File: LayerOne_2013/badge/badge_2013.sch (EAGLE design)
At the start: 125 parts, among them CON2 EXT, CON6 J8, CON8 J3, IC1 SLICE_NOSHIFT_TLC5947HTSSOP32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, IC3 SLICE_NOSHIFT_TLC5947HTSSOP32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, IC4 TL064D, K1 5-XX, K2 5-XX, K3 5-XX, K4 5-XX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

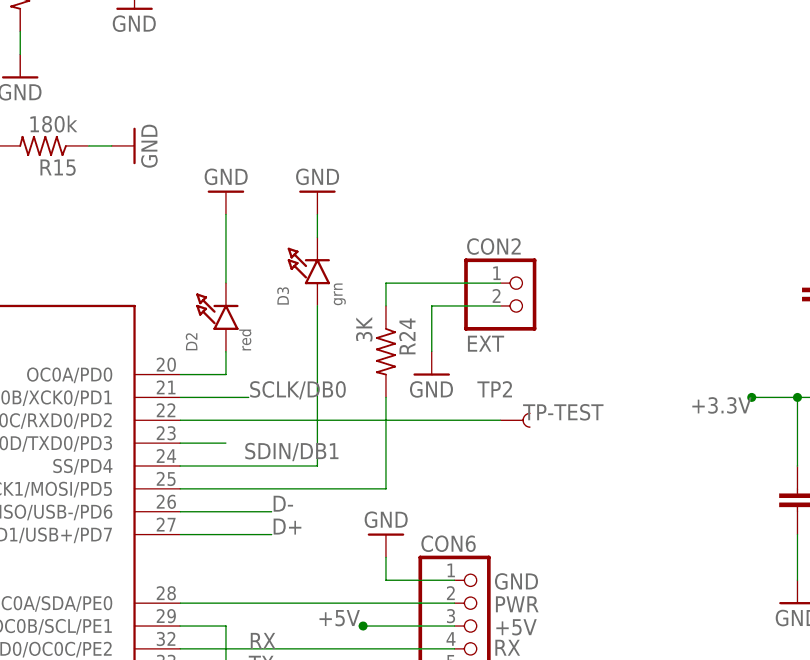
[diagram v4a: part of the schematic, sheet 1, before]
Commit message: 
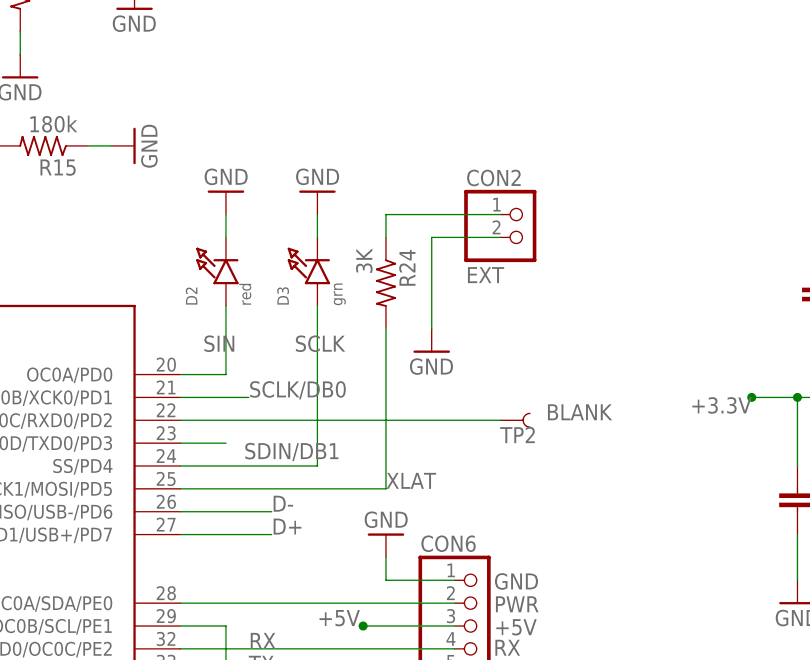
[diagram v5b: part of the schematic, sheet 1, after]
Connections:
- removed net N$19: IC2.XCK1/MOSI/PD5, R24.2
- removed net N$21: D2.A, IC2.OC0A/PD0
- removed net N$22: D3.A, IC2.SS/PD4
- removed net TP-TEST: IC2.OC0C/RXD0/PD2, TP2.1
- net BLANK: now also IC2.OC0C/RXD0/PD2, TP2.1
- net SCLK: now also D3.A, IC2.SS/PD4
- net SIN: now also D2.A, IC2.OC0A/PD0
- net XLAT: now also IC2.XCK1/MOSI/PD5, R24.2
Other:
- moved on the sheet: CON2, D2, R24
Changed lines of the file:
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@@
 </instance>
 <instance part="+3.3V" gate="1" x="246.38" y="86.36"/>
-<instance part="CON2" gate="G$1" x="241.3" y="137.16"/>
+<instance part="CON2" gate="G$1" x="241.3" y="144.78"/>
 <instance part="C1" gate="G$1" x="332.74" y="170.18" rot="R180"/>
 <instance part="C3" gate="G$1" x="93.98" y="226.06" rot="R270"/>
@@
 <instance part="CH1" gate="G$1" x="264.16" y="215.9"/>
 <instance part="TP1" gate="G$1" x="83.82" y="193.04"/>
-<instance part="TP2" gate="G$1" x="238.76" y="124.46"/>
+<instance part="TP2" gate="G$1" x="238.76" y="124.46" smashed="yes">
+<attribute name="NAME" x="238.76" y="121.92" size="1.778" layer="95"/>
+<attribute name="VALUE" x="236.22" y="121.92" size="1.778" layer="96"/>
+</instance>
 <instance part="Z1" gate="G$1" x="93.98" y="114.3" rot="MR0"/>
 <instance part="GND7" gate="1" x="99.06" y="99.06"/>
 <instance part="GND8" gate="1" x="78.74" y="129.54" rot="R180"/>
-<instance part="D2" gate="G$1" x="208.28" y="137.16" rot="R90"/>
+<instance part="D2" gate="G$1" x="208.28" y="142.24" rot="R90"/>
 <instance part="D3" gate="G$1" x="218.44" y="142.24" rot="R90"/>
 <instance part="GND9" gate="1" x="208.28" y="149.86" rot="R180"/>
@@
 <instance part="C23" gate="G$1" x="66.04" y="43.18" rot="R270"/>
 <instance part="GND40" gate="1" x="48.26" y="50.8"/>
-<instance part="GND41" gate="1" x="231.14" y="129.54"/>
+<instance part="GND41" gate="1" x="231.14" y="132.08"/>
 <instance part="X2" gate="G$1" x="121.92" y="60.96" smashed="yes" rot="R90">
 <attribute name="VALUE" x="137.668" y="59.182" size="1.778" layer="96" rot="R180"/>
@@
 <instance part="GND47" gate="1" x="312.42" y="187.96" rot="R270"/>
 <instance part="SJ1" gate="1" x="269.24" y="91.44"/>
-<instance part="R24" gate="G$1" x="226.06" y="132.08" rot="R270"/>
+<instance part="R24" gate="G$1" x="226.06" y="139.7" rot="R270"/>
 <instance part="PDI" gate="G$1" x="134.62" y="147.32" rot="R90"/>
 <instance part="R22" gate="G$1" x="81.28" y="33.02" rot="R270"/>
@@
 <segment>
 <pinref part="D2" gate="G$1" pin="C"/>
-<wire x1="208.28" y1="139.7" x2="208.28" y2="147.32" width="0.1524" layer="91"/>
+<wire x1="208.28" y1="144.78" x2="208.28" y2="147.32" width="0.1524" layer="91"/>
 <pinref part="GND9" gate="1" pin="GND"/>
 </segment>
@@
 <segment>
 <pinref part="CON2" gate="G$1" pin="2"/>
-<wire x1="238.76" y1="137.16" x2="231.14" y2="137.16" width="0.1524" layer="91"/>
-<wire x1="231.14" y1="137.16" x2="231.14" y2="132.08" width="0.1524" layer="91"/>
+<wire x1="238.76" y1="144.78" x2="231.14" y2="144.78" width="0.1524" layer="91"/>
+<wire x1="231.14" y1="144.78" x2="231.14" y2="134.62" width="0.1524" layer="91"/>
 <pinref part="GND41" gate="1" pin="GND"/>
 </segment>
@@
 </segment>
 </net>
-<net name="N$19" class="0">
+<net name="XLAT" class="0">
 <segment>
 <pinref part="IC2" gate="G$1" pin="XCK1/MOSI/PD5"/>
 <wire x1="203.2" y1="116.84" x2="226.06" y2="116.84" width="0.1524" layer="91"/>
 <pinref part="R24" gate="G$1" pin="2"/>
-<wire x1="226.06" y1="127" x2="226.06" y2="116.84" width="0.1524" layer="91"/>
+<wire x1="226.06" y1="134.62" x2="226.06" y2="116.84" width="0.1524" layer="91"/>
+<label x="226.06" y="116.84" size="1.778" layer="95"/>
 </segment>
 </net>
@@
 </segment>
 </net>
-<net name="N$21" class="0">
+<net name="SIN" class="0">
 <segment>
 <pinref part="D2" gate="G$1" pin="A"/>
 <pinref part="IC2" gate="G$1" pin="OC0A/PD0"/>
-<wire x1="208.28" y1="132.08" x2="208.28" y2="129.54" width="0.1524" layer="91"/>
+<wire x1="208.28" y1="137.16" x2="208.28" y2="129.54" width="0.1524" layer="91"/>
 <wire x1="208.28" y1="129.54" x2="203.2" y2="129.54" width="0.1524" layer="91"/>
-</segment>
-</net>
-<net name="N$22" class="0">
+<label x="205.74" y="132.08" size="1.778" layer="95"/>
+</segment>
+</net>
+<net name="SCLK" class="0">
 <segment>
 <pinref part="D3" gate="G$1" pin="A"/>
@@
 <wire x1="218.44" y1="137.16" x2="218.44" y2="119.38" width="0.1524" layer="91"/>
 <wire x1="218.44" y1="119.38" x2="203.2" y2="119.38" width="0.1524" layer="91"/>
+<label x="215.9" y="132.08" size="1.778" layer="95"/>
 </segment>
 </net>
@@
 </segment>
 </net>
-<net name="TP-TEST" class="0">
+<net name="BLANK" class="0">
 <segment>
 <pinref part="IC2" gate="G$1" pin="OC0C/RXD0/PD2"/>
 <pinref part="TP2" gate="G$1" pin="1"/>
 <wire x1="203.2" y1="124.46" x2="238.76" y2="124.46" width="0.1524" layer="91"/>
-<label x="241.3" y="124.46" size="1.778" layer="95"/>
+<label x="243.84" y="124.46" size="1.778" layer="95"/>
 </segment>
 </net>
@@
 <segment>
 <pinref part="CON2" gate="G$1" pin="1"/>
-<wire x1="238.76" y1="139.7" x2="226.06" y2="139.7" width="0.1524" layer="91"/>
+<wire x1="238.76" y1="147.32" x2="226.06" y2="147.32" width="0.1524" layer="91"/>
 <pinref part="R24" gate="G$1" pin="1"/>
-<wire x1="226.06" y1="137.16" x2="226.06" y2="139.7" width="0.1524" layer="91"/>
-</segment>
-</net>
+<wire x1="226.06" y1="144.78" x2="226.06" y2="147.32" width="0.1524" layer="91"/>
+</segment>
+</net>

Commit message: 
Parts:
- removed JP6: USB-RECEPTABLE, daspilker:USB-RECEPTABLE
- added USB1: (no value), adafruit:USBMINIB
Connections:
- net +5V: now also USB1.VBUS; no longer JP6.VCC
- net D+: now also USB1.D+; no longer JP6.D+
- net D-: now also USB1.D-; no longer JP6.D-
- net GND: now also USB1.GND; no longer JP6.GND
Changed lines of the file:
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@@
 </variantdefs>
 <classes>
-<class number="0" name="default" width="0" drill="0">
+<class number="0" name="default" width="0.254" drill="0.3048">
+<clearance class="0" value="0.1524"/>
 </class>
 </classes>
@@
 <part name="Z1" library="USBug" deviceset="PRTR5V0U2X" device=""/>
 <part name="GND7" library="SparkFun" deviceset="GND" device=""/>
-<part name="GND8" library="SparkFun" deviceset="GND" device=""/>
 <part name="D2" library="microbuilder" deviceset="LED" device="0805" value="red"/>
 <part name="D3" library="microbuilder" deviceset="LED" device="0805" value="grn"/>
@@
 <part name="C12" library="SparkFun" deviceset="CAP" device="0805" value="0.1uF"/>
 <part name="GND11" library="SparkFun" deviceset="GND" device=""/>
-<part name="JP6" library="daspilker" deviceset="USB-RECEPTABLE" device=""/>
 <part name="GND12" library="SparkFun" deviceset="GND" device=""/>
 <part name="GND13" library="SparkFun" deviceset="GND" device=""/>
@@
 <part name="PDI" library="microbuilder" deviceset="HEADER-1X2" device="" value="CON6"/>
 <part name="R22" library="resistor" deviceset="R-US_" device="R0805" value="180K"/>
+<part name="USB1" library="adafruit" deviceset="USB" device="MINIB"/>
 </parts>
 <sheets>
@@
 <instance part="Z1" gate="G$1" x="93.98" y="114.3" rot="MR0"/>
 <instance part="GND7" gate="1" x="99.06" y="99.06"/>
-<instance part="GND8" gate="1" x="78.74" y="129.54" rot="R180"/>
 <instance part="D2" gate="G$1" x="208.28" y="142.24" rot="R90"/>
 <instance part="D3" gate="G$1" x="218.44" y="142.24" rot="R90"/>
@@
 <instance part="C12" gate="G$1" x="213.36" y="86.36" rot="R90"/>
 <instance part="GND11" gate="1" x="226.06" y="86.36" rot="R90"/>
-<instance part="JP6" gate="G$1" x="66.04" y="114.3" rot="R180"/>
 <instance part="GND12" gate="1" x="287.02" y="121.92" rot="R270"/>
 <instance part="GND13" gate="1" x="284.48" y="114.3" rot="R270"/>
@@
 <instance part="PDI" gate="G$1" x="134.62" y="147.32" rot="R90"/>
 <instance part="R22" gate="G$1" x="81.28" y="33.02" rot="R270"/>
+<instance part="USB1" gate="G$1" x="66.04" y="124.46"/>
 </instances>
 <busses>
@@
 </segment>
 <segment>
-<wire x1="73.66" y1="119.38" x2="78.74" y2="119.38" width="0.1524" layer="91"/>
-<wire x1="78.74" y1="119.38" x2="78.74" y2="127" width="0.1524" layer="91"/>
-<pinref part="GND8" gate="1" pin="GND"/>
-<pinref part="JP6" gate="G$1" pin="GND"/>
-</segment>
-<segment>
 <pinref part="U1" gate="G$1" pin="NC(GND)@1"/>
 <wire x1="299.72" y1="139.7" x2="297.18" y2="139.7" width="0.1524" layer="91"/>
@@
 <pinref part="GND47" gate="1" pin="GND"/>
 <wire x1="314.96" y1="187.96" x2="317.5" y2="187.96" width="0.1524" layer="91"/>
+</segment>
+<segment>
+<pinref part="USB1" gate="G$1" pin="GND"/>
+<wire x1="76.2" y1="119.38" x2="81.28" y2="119.38" width="0.1524" layer="91"/>
 </segment>
 </net>
@@
 </segment>
 <segment>
-<wire x1="73.66" y1="109.22" x2="78.74" y2="109.22" width="0.1524" layer="91"/>
-<wire x1="78.74" y1="109.22" x2="78.74" y2="99.06" width="0.1524" layer="91"/>
-<pinref part="JP6" gate="G$1" pin="VCC"/>
-<label x="79.502" y="92.964" size="1.778" layer="95" rot="R90"/>
-<junction x="78.74" y="99.06"/>
-</segment>
-<segment>
 <pinref part="Z1" gate="G$1" pin="P$4"/>
 <wire x1="99.06" y1="121.92" x2="99.06" y2="129.54" width="0.1524" layer="91"/>
@@
 <junction x="99.06" y="129.54"/>
 </segment>
+<segment>
+<pinref part="USB1" gate="G$1" pin="VBUS"/>
+<wire x1="76.2" y1="129.54" x2="81.28" y2="129.54" width="0.1524" layer="91"/>
+</segment>
 </net>
 <net name="D-" class="0">
@@
 </segment>
 <segment>
-<wire x1="73.66" y1="111.76" x2="78.74" y2="111.76" width="0.1524" layer="91"/>
-<pinref part="JP6" gate="G$1" pin="D-"/>
-<label x="79.248" y="110.998" size="1.778" layer="95"/>
-</segment>
-<segment>
 <pinref part="IC2" gate="G$1" pin="RXD1/MISO/USB-/PD6"/>
 <wire x1="203.2" y1="114.3" x2="213.36" y2="114.3" width="0.1524" layer="91"/>
 <label x="213.36" y="114.3" size="1.778" layer="95"/>
+</segment>
+<segment>
+<pinref part="USB1" gate="G$1" pin="D-"/>
+<wire x1="76.2" y1="124.46" x2="81.28" y2="124.46" width="0.1524" layer="91"/>
 </segment>
 </net>
@@
 </segment>
 <segment>
-<wire x1="73.66" y1="114.3" x2="78.74" y2="114.3" width="0.1524" layer="91"/>
-<pinref part="JP6" gate="G$1" pin="D+"/>
-<label x="79.248" y="113.792" size="1.778" layer="95"/>
-</segment>
-<segment>
 <pinref part="IC2" gate="G$1" pin="TXD1/USB+/PD7"/>
 <wire x1="203.2" y1="111.76" x2="213.36" y2="111.76" width="0.1524" layer="91"/>
 <label x="213.36" y="111.76" size="1.778" layer="95"/>
 </segment>
-</net>
+<segment>
+<pinref part="USB1" gate="G$1" pin="D+"/>
+<wire x1="76.2" y1="127" x2="81.28" y2="127" width="0.1524" layer="91"/>
+</segment>
+</net>

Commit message: 
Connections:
- net BLANK: now also D3.A, IC2.SS/PD4; no longer IC2.OC0C/RXD0/PD2, TP2.1
- net SCLK: now also IC2.OC0C/RXD0/PD2, TP2.1; no longer D3.A, IC2.SS/PD4
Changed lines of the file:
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@@
-</segment>
-</net>
-<net name="SCLK" class="0">
-<segment>
-<pinref part="D3" gate="G$1" pin="A"/>
-<pinref part="IC2" gate="G$1" pin="SS/PD4"/>
-<wire x1="218.44" y1="137.16" x2="218.44" y2="119.38" width="0.1524" layer="91"/>
-<wire x1="218.44" y1="119.38" x2="203.2" y2="119.38" width="0.1524" layer="91"/>
-<label x="215.9" y="132.08" size="1.778" layer="95"/>
 </segment>
 </net>
@@
 <pinref part="C13" gate="G$1" pin="1"/>
 <wire x1="299.72" y1="71.12" x2="274.32" y2="71.12" width="0.1524" layer="91"/>
-</segment>
-</net>
-<net name="BLANK" class="0">
-<segment>
-<pinref part="IC2" gate="G$1" pin="OC0C/RXD0/PD2"/>
-<pinref part="TP2" gate="G$1" pin="1"/>
-<wire x1="203.2" y1="124.46" x2="238.76" y2="124.46" width="0.1524" layer="91"/>
-<label x="243.84" y="124.46" size="1.778" layer="95"/>
 </segment>
 </net>
@@
 </segment>
 </net>
+<net name="BLANK" class="0">
+<segment>
+<pinref part="D3" gate="G$1" pin="A"/>
+<pinref part="IC2" gate="G$1" pin="SS/PD4"/>
+<wire x1="218.44" y1="137.16" x2="218.44" y2="119.38" width="0.1524" layer="91"/>
+<wire x1="218.44" y1="119.38" x2="203.2" y2="119.38" width="0.1524" layer="91"/>
+<label x="215.9" y="132.08" size="1.778" layer="95"/>
+</segment>
+</net>
+<net name="SCLK" class="0">
+<segment>
+<pinref part="IC2" gate="G$1" pin="OC0C/RXD0/PD2"/>
+<pinref part="TP2" gate="G$1" pin="1"/>
+<wire x1="203.2" y1="124.46" x2="238.76" y2="124.46" width="0.1524" layer="91"/>
+<label x="243.84" y="124.46" size="1.778" layer="95"/>
+</segment>
+</net>
